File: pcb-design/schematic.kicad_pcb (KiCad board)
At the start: 2 copper layers, 80 parts, among them J1 TempGauge, J2 FuelGauge, J3 SpeedInput_C2_P10-13, J5 SpeedInput_C2_P10-13, J6 SpeedInput_C2_P10-13, Q1 2N2222, Q2 2N2222, Q3 2N2222, Q6 2N2222, Q7 2N2222, Q8 2N3906, Q9 2N3906, U1 ESP32-WROOM-32, U2 MCP23017_SP, U3 MCP2562-E-P

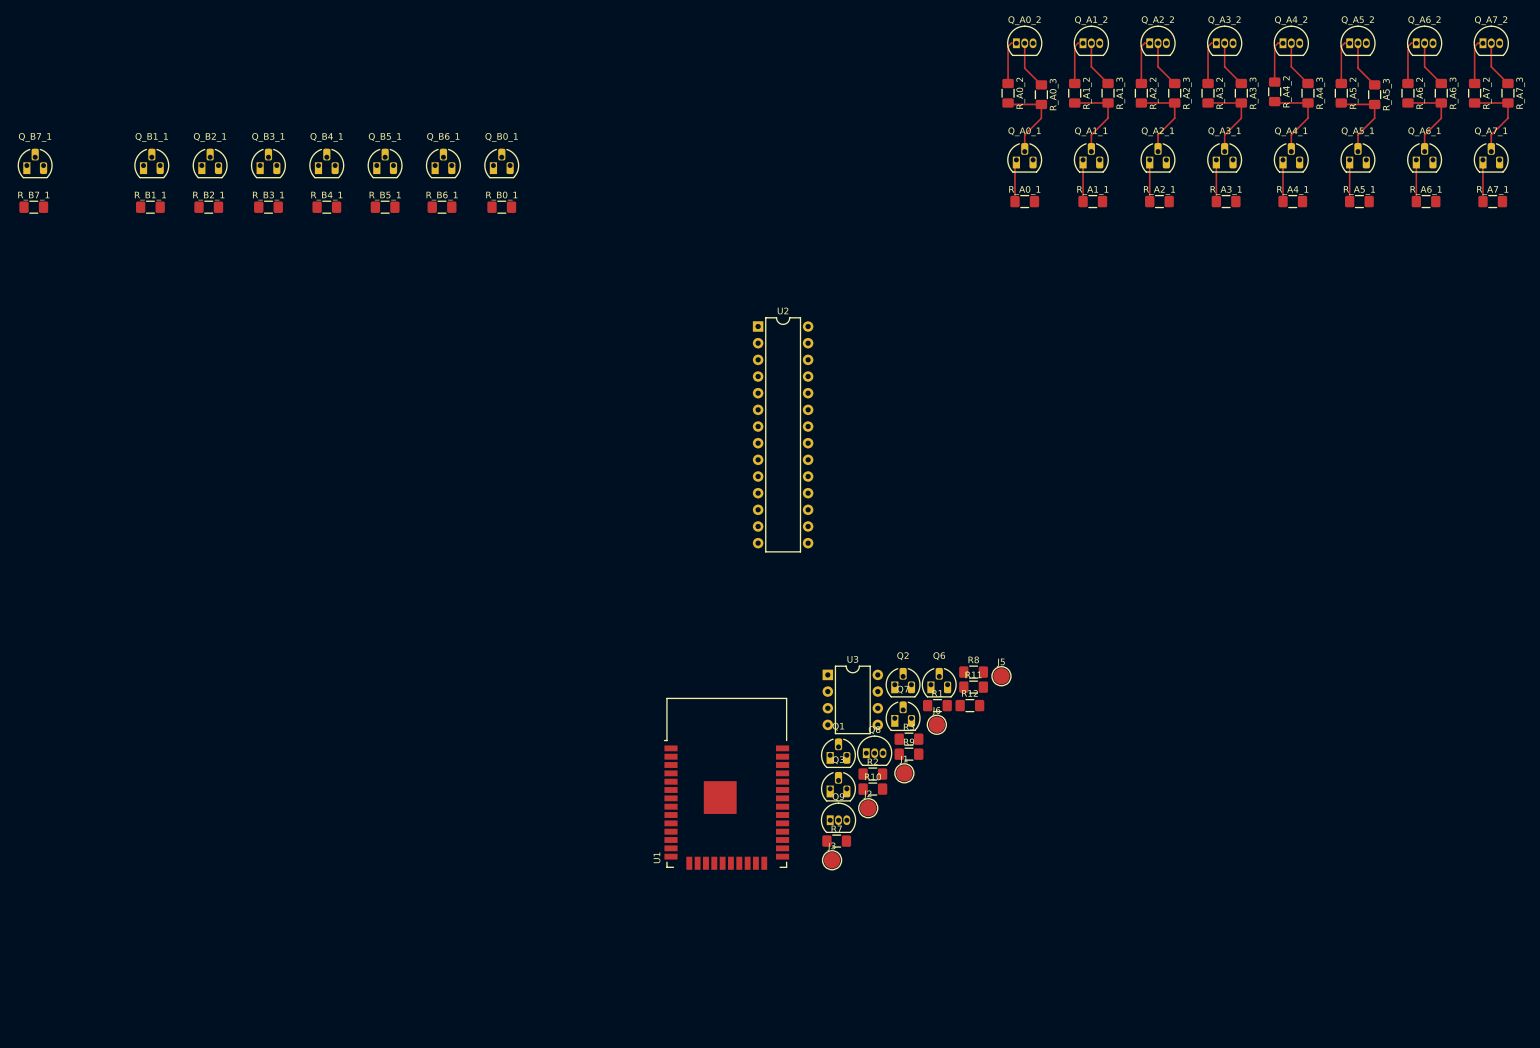
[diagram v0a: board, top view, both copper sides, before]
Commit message: Swapped the esp32 symbol and footprint to be one for the dev modules so I can just populate the boards with standoffs.
Wired up some more nets and made the layout a little prettier.
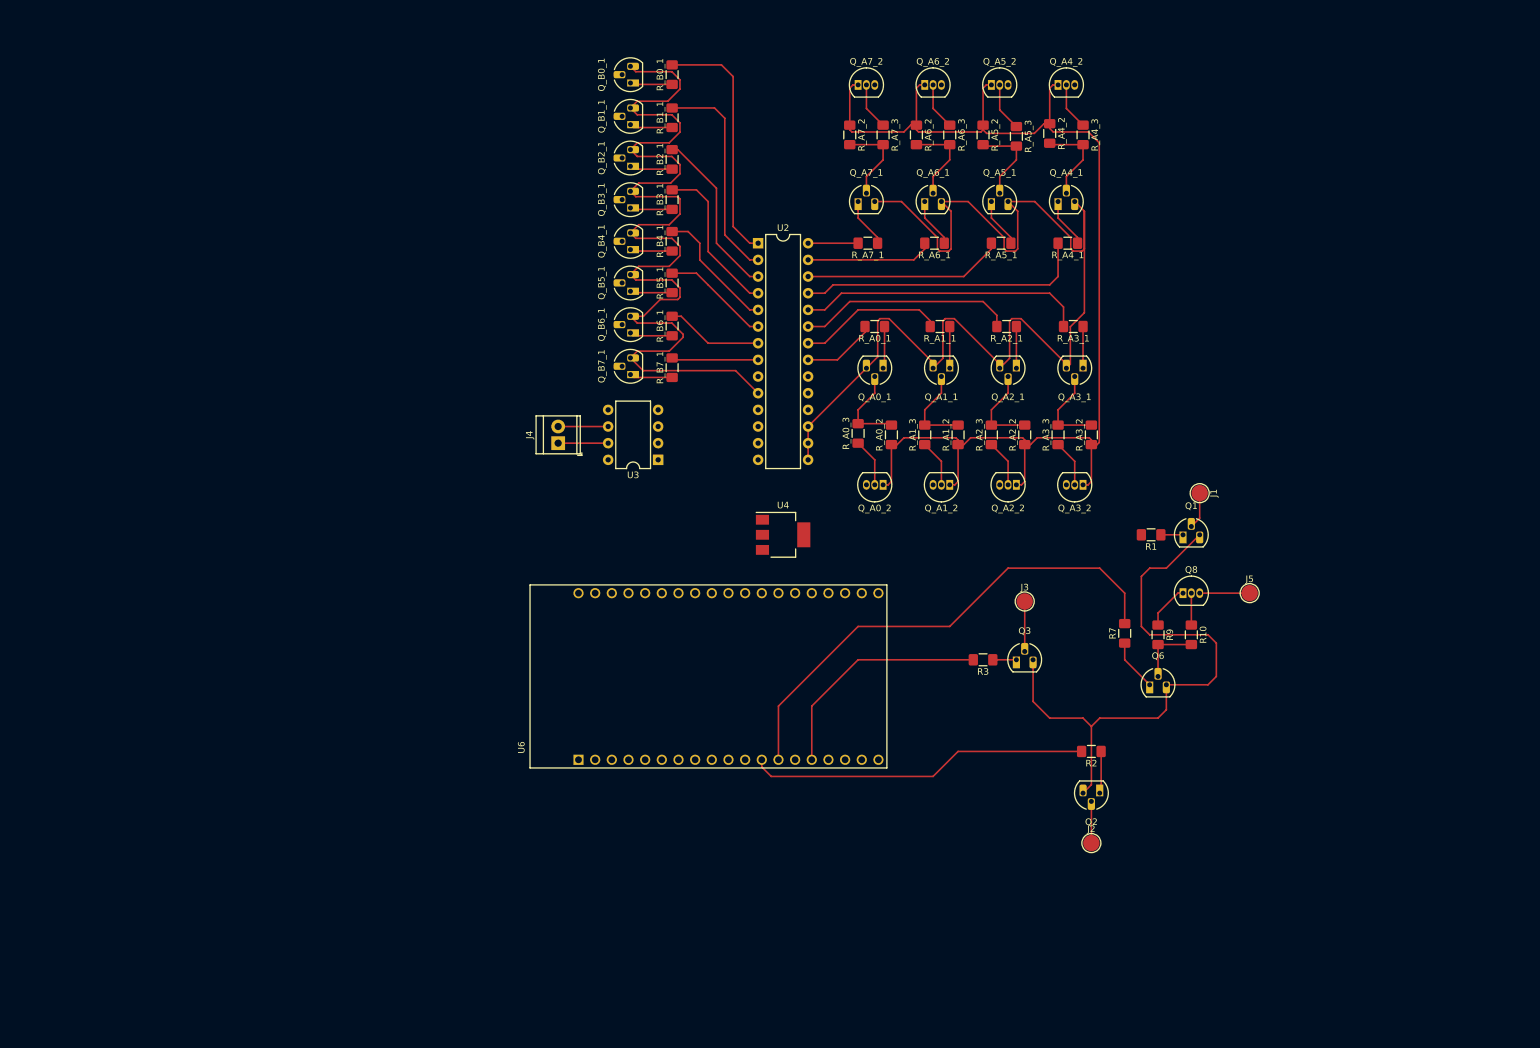
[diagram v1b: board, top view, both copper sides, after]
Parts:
- removed J6: SpeedInput_C2_P10-13, TestPoint:TestPoint_Pad_D2.5mm
- removed Q7: 2N2222, Package_TO_SOT_THT:TO-92_HandSolder
- removed Q9: 2N3906, Package_TO_SOT_THT:TO-92_Inline
- removed R11: 22000, Resistor_SMD:R_1206_3216Metric_Pad1.42x1.75mm_HandSolder
- removed R12, R8: 4000, Resistor_SMD:R_1206_3216Metric_Pad1.42x1.75mm_HandSolder
- removed U1: ESP32-WROOM-32, RF_Module:ESP32-WROOM-32
- added J4: Screw_Terminal_01x02, TerminalBlock_TE-Connectivity:TerminalBlock_TE_282834-2_1x02_P2.54mm_Horizontal, F.Cu at (113.0, 81.3)
- added U4: AP1117-33, Package_TO_SOT_SMD:SOT-223-3_TabPin2, F.Cu at (147.3, 95.2)
- added U6: ESP32-DEVKITC-32D, MODULE_ESP32-DEVKITC-32D, F.Cu at (135.9, 116.8)
- J3: value SpeedInput_C2_P10-13 -> SpeedometerOutput
- J5: value SpeedInput_C2_P10-13 -> TachometerOutput
- moved R_B7_1 100.3 mm to (130.4, 69.8), turned to 90 degrees
- moved Q_B7_1 97.4 mm to (124.1, 70.8), turned to 90 degrees
- moved Q_A7_1 95.5 mm to (158.8, 44.5)
- moved Q_A7_2 95.5 mm to (158.8, 26.7)
- moved R_A7_1 95.5 mm to (160.2, 50.8), turned to 180 degrees
- moved R_A7_2 95.5 mm to (157.5, 34.3)
- moved R_A7_3 95.5 mm to (162.6, 34.3)
- moved R_B1_1 80.7 mm to (130.4, 31.7), turned to 90 degrees
- moved Q_A6_1 75.2 mm to (168.9, 44.5)
- moved Q_A6_2 75.2 mm to (168.9, 26.7)
- moved R_A6_2 75.2 mm to (167.6, 34.3)
- moved R_A6_3 75.2 mm to (172.7, 34.3)
- moved R_A6_1 75.2 mm to (170.4, 50.8), turned to 180 degrees
- moved Q_B1_1 74.5 mm to (124.1, 32.7), turned to 90 degrees
- moved R_B2_1 71.0 mm to (130.4, 38.0), turned to 90 degrees
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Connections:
- R3 pad 2: SpeedometerOutput -> SpeedometerSignal
- U2 pad 12: /Indicator_Lights/SCK -> I2C0_SCK
- U2 pad 13: /Indicator_Lights/SDA -> I2C0_SDA
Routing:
- net GND: track 0.00 -> 415.4 mm
- net +12V: track 56.7 -> 188.4 mm
- net TachometerOutput: track 0.00 -> 75.9 mm
- net FuelOutput: track 0.00 -> 52.0 mm
- net Net-(R_A4_1-Pad2): track 0.00 -> 44.2 mm
- net Net-(R_A3_1-Pad2): track 0.00 -> 43.8 mm
- net Net-(R_B0_1-Pad2): track 0.00 -> 37.8 mm
- net SpeedometerSignal: track 0.00 -> 35.7 mm
- net Net-(R_B1_1-Pad2): track 0.00 -> 33.1 mm
- net Net-(R_A2_1-Pad2): track 0.00 -> 32.9 mm
- net Net-(R_A5_1-Pad2): track 0.00 -> 30.6 mm
- net Net-(R_B2_1-Pad2): track 0.00 -> 26.0 mm
- net Net-(R_B3_1-Pad2): track 0.00 -> 24.1 mm
- net Net-(R_A1_1-Pad2): track 0.00 -> 22.3 mm
- net Net-(R_B4_1-Pad2): track 0.00 -> 19.5 mm
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
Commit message: checkin
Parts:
- moved U4 63.8 mm to (95.2, 132.1)
- moved J2 19.8 mm to (208.3, 156.2)
- moved Q2 19.8 mm to (209.6, 148.6)
- moved R2 19.8 mm to (208.3, 142.2)
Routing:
- net ESP_CAN0_RX: track 0.00 -> 68.1 mm
- net ESP_CAN0_TX: track 0.00 -> 62.0 mm
- net TemperatureOutput: track 0.00 -> 51.4 mm
- net +3V3: track 0.00 -> 41.3 mm
- net I2C0_SCK: track 0.00 -> 34.6 mm
- net I2C0_SDA: track 0.00 -> 28.9 mm
- net FuelOutput: track 52.0 -> 33.2 mm
- net SpeedometerSignal: track 35.7 -> 18.2 mm
- net GND: track 415.4 -> 411.3 mm, vias 0 -> 1

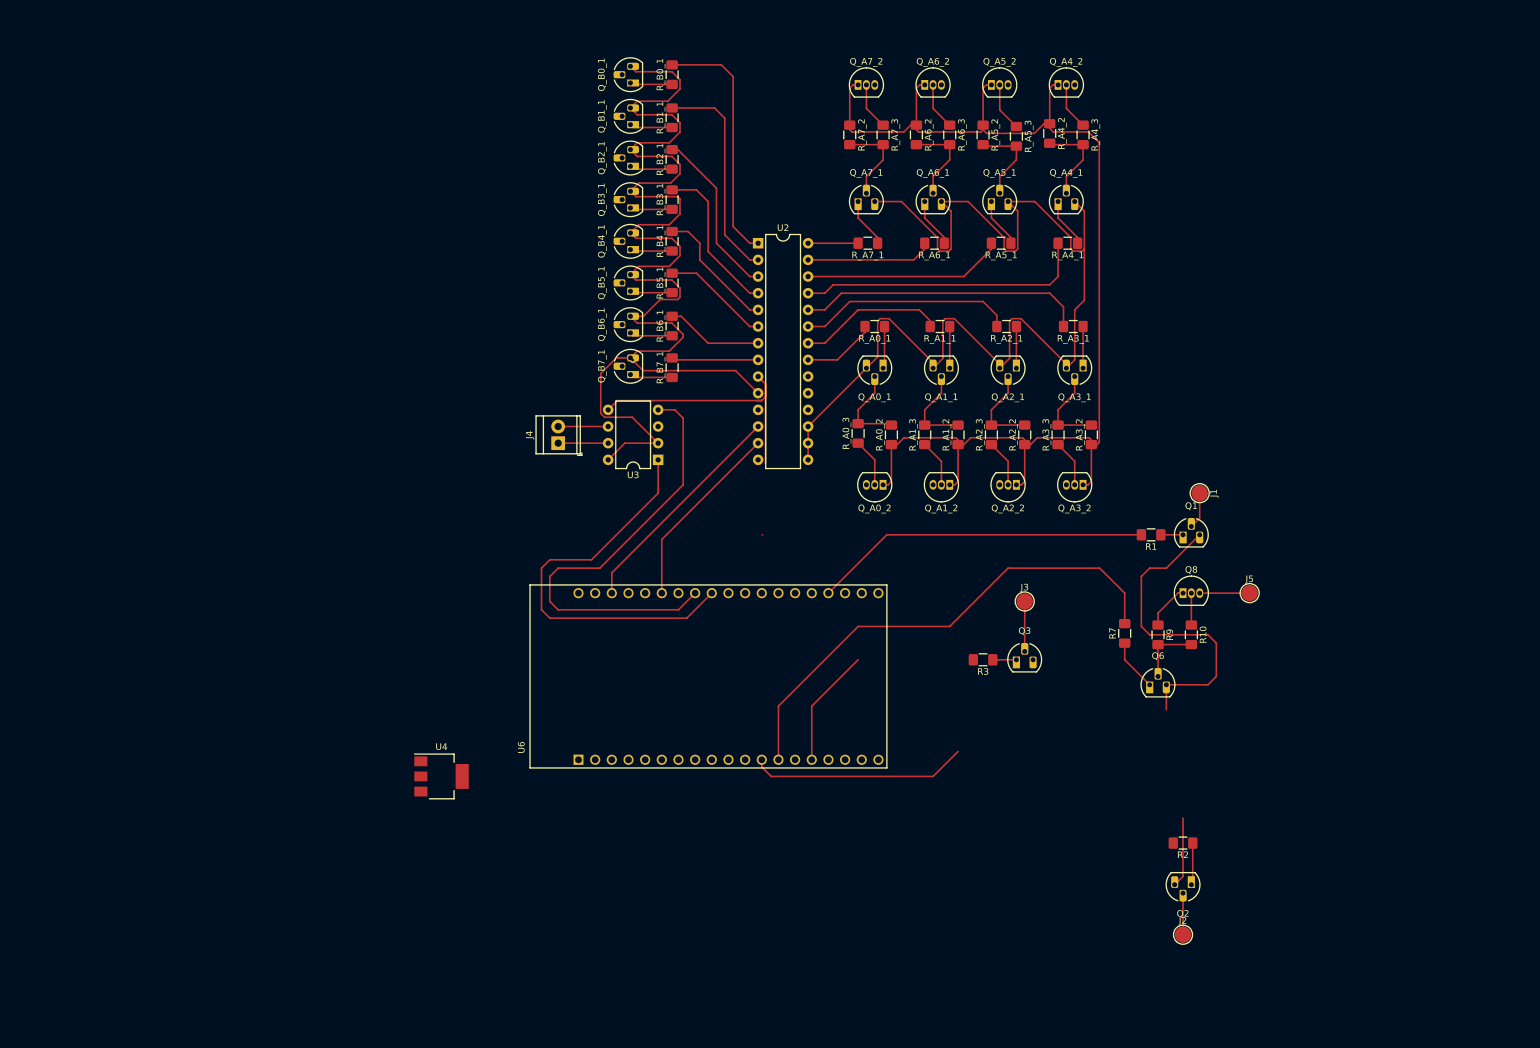
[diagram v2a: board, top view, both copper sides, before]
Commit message: Added TE 827881-1 connector and footprint re-arranged schematic
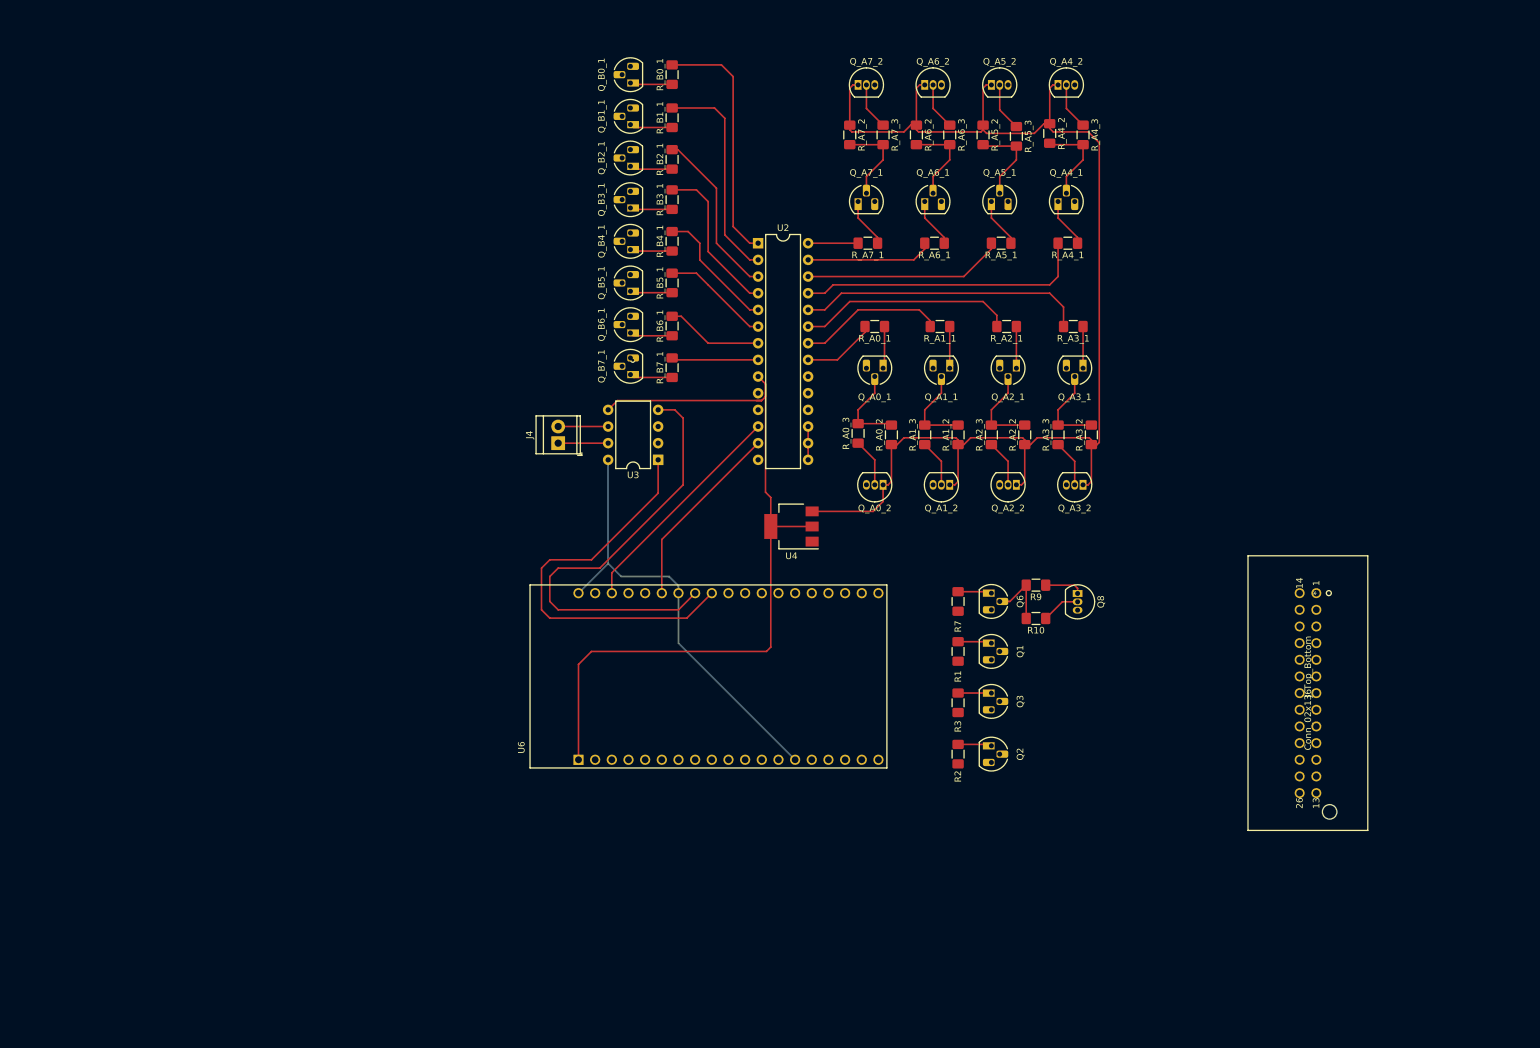
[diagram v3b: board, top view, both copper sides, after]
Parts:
- removed J1: TempGauge, TestPoint:TestPoint_Pad_D2.5mm
- removed J2: FuelGauge, TestPoint:TestPoint_Pad_D2.5mm
- removed J3: SpeedometerOutput, TestPoint:TestPoint_Pad_D2.5mm
- removed J5: TachometerOutput, TestPoint:TestPoint_Pad_D2.5mm
- added J6: Conn_02x13_Top_Bottom, pcb-design:Connector_TE_827881-1, F.Cu at (228.6, 104.1)
- moved U4 65.5 mm to (148.6, 94.0), turned to 180 degrees
- moved Q2 37.1 mm to (179.1, 127.4), turned to 270 degrees
- moved R2 36.9 mm to (174.0, 128.7), turned to 270 degrees
- moved R1 34.4 mm to (174.0, 113.0), turned to 270 degrees
- moved Q1 33.6 mm to (179.1, 111.8), turned to 270 degrees
- moved Q6 27.9 mm to (179.1, 104.1), turned to 270 degrees
- moved R7 25.9 mm to (174.0, 105.4), turned to 270 degrees
- moved R10 23.8 mm to (185.9, 108.0), turned to 180 degrees
- moved R9 20.1 mm to (185.9, 102.9), turned to 180 degrees
- moved Q8 16.1 mm to (192.2, 104.2), turned to 270 degrees
- moved R3 7.58 mm to (174.0, 120.9), turned to 270 degrees
- moved Q3 6.35 mm to (179.1, 119.4), turned to 270 degrees
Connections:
- net Net-(J4-Pad1) renamed CAN0_H
- net Net-(J4-Pad2) renamed CAN0_L
- Q1 pad 2: Net-(J1-Pad1) -> TempGauge
- Q2 pad 2: Net-(J2-Pad1) -> FuelGauge
- Q3 pad 2: Net-(J3-Pad1) -> Speedometer
- Q8 pad 3: Net-(J5-Pad1) -> Tachometer
- Q_A0_2 pad 3: /Indicator_Lights/A0_SourceOutput -> A0_SourceOutput
- Q_A1_2 pad 3: /Indicator_Lights/A1_SourceOutput -> A1_SourceOutput
- Q_A2_2 pad 3: /Indicator_Lights/A2_SourceOutput -> A2_SourceOutput
- Q_A3_2 pad 3: /Indicator_Lights/A3_SourceOutput -> A3_SourceOutput
- Q_A4_2 pad 3: /Indicator_Lights/A4_SourceOutput -> A4_SourceOutput
- Q_A5_2 pad 3: /Indicator_Lights/A5_SourceOutput -> A5_SourceOutput
- Q_A6_2 pad 3: /Indicator_Lights/A6_SourceOutput -> A6_SourceOutput
- Q_A7_2 pad 3: /Indicator_Lights/A7_SourceOutput -> A7_SourceOutput
- Q_B0_1 pad 2: /Indicator_Lights/B0_SinkOutput -> B0_SinkOutput
- Q_B1_1 pad 2: /Indicator_Lights/B1_SinkOutput -> B1_SinkOutput
- Q_B2_1 pad 2: /Indicator_Lights/B2_SinkOutput -> B2_SinkOutput
- Q_B3_1 pad 2: /Indicator_Lights/B3_SinkOutput -> B3_SinkOutput
- Q_B4_1 pad 2: /Indicator_Lights/B4_SinkOutput -> B4_SinkOutput
- Q_B5_1 pad 2: /Indicator_Lights/B5_SinkOutput -> B5_SinkOutput
- Q_B6_1 pad 2: /Indicator_Lights/B6_SinkOutput -> B6_SinkOutput
- Q_B7_1 pad 2: /Indicator_Lights/B7_SinkOutput -> B7_SinkOutput
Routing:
- net GND: track 411.3 -> 75.9 mm
- net +3V3: track 41.3 -> 120.8 mm
- net TachometerOutput: track 75.9 -> 0.00 mm
- net TemperatureOutput: track 51.4 -> 0.00 mm
- net FuelOutput: track 33.2 -> 0.00 mm
- net SpeedometerSignal: track 18.2 -> 0.00 mm
- net +12V: track 188.4 -> 201.3 mm
- net Net-(J5-Pad1): track 7.62 -> 0.00 mm
- net Net-(J3-Pad1): track 7.62 -> 0.00 mm
- net Net-(J2-Pad1): track 6.35 -> 0.00 mm
- net Net-(J1-Pad1): track 5.61 -> 0.00 mm
- net Net-(Q6-Pad1): track 7.93 -> 5.17 mm
- net Net-(Q1-Pad1): track 3.38 -> 5.17 mm
- net Net-(Q3-Pad1): track 3.59 -> 5.09 mm
- net Net-(Q2-Pad1): track 6.44 -> 5.17 mm
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
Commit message: Final changes for Rev 1 board, ordered 10/06/2020
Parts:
- added U7: L7805, Package_SIP:SIP3_11.6x8.5mm, F.Cu at (96.5, 147.3)
- U4: footprint Package_TO_SOT_SMD:SOT-223-3_TabPin2 -> Package_SIP:SIP3_11.6x8.5mm
- moved J4 80.8 mm to (136.6, 158.6), turned to 180 degrees
- moved J6 72.3 mm to (160.0, 127.0)
- moved Q1 70.8 mm to (119.4, 149.9)
- moved R1 70.8 mm to (114.3, 151.1)
- moved U6 67.3 mm to (69.8, 129.5), turned to 180 degrees
- moved R10 63.9 mm to (126.2, 130.9)
- moved R7 63.9 mm to (114.3, 128.3)
- moved R3 63.9 mm to (114.3, 143.7)
- moved R9 63.9 mm to (126.2, 125.8)
- moved Q3 63.9 mm to (119.4, 142.2)
- moved Q6 63.9 mm to (119.4, 127.0)
- moved Q8 63.9 mm to (132.5, 127.1)
- moved R_B4_1 61.9 mm to (74.5, 77.2)
- moved R_A0_2 61.9 mm to (108.0, 106.7)
- moved R_A1_2 61.9 mm to (118.1, 106.7)
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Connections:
- J6 pad 1: A0_SourceOutput -> B0_SinkOutput
- J6 pad 14: B0_SinkOutput -> A7_SourceOutput
- J6 pad 15: B1_SinkOutput -> A6_SourceOutput
- J6 pad 16: B2_SinkOutput -> A5_SourceOutput
- J6 pad 17: B3_SinkOutput -> A4_SourceOutput
- J6 pad 18: B4_SinkOutput -> A3_SourceOutput
- J6 pad 19: B5_SinkOutput -> A2_SourceOutput
- J6 pad 2: A1_SourceOutput -> B1_SinkOutput
- J6 pad 20: B6_SinkOutput -> A1_SourceOutput
- J6 pad 21: B7_SinkOutput -> A0_SourceOutput
- J6 pad 22: TempGauge -> Tachometer
- J6 pad 23: Tachometer -> FuelGauge
- J6 pad 25: FuelGauge -> TempGauge
- J6 pad 3: A2_SourceOutput -> B2_SinkOutput
- J6 pad 4: A3_SourceOutput -> B3_SinkOutput
- J6 pad 5: A4_SourceOutput -> B4_SinkOutput
- J6 pad 6: A5_SourceOutput -> B5_SinkOutput
- J6 pad 7: A6_SourceOutput -> B6_SinkOutput
- J6 pad 8: A7_SourceOutput -> B7_SinkOutput
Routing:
- net B7_SinkOutput: track 0.00 -> 278.3 mm
- net B6_SinkOutput: track 0.00 -> 264.0 mm
- net B5_SinkOutput: track 0.00 -> 249.8 mm
- net B4_SinkOutput: track 0.00 -> 235.5 mm
- net B3_SinkOutput: track 0.00 -> 221.2 mm
- net B2_SinkOutput: track 0.00 -> 206.9 mm
- net B1_SinkOutput: track 0.00 -> 192.7 mm
- net B0_SinkOutput: track 0.00 -> 173.1 mm
- net A7_SourceOutput: track 0.00 -> 135.8 mm
- net A6_SourceOutput: track 0.00 -> 124.1 mm
- net +12V: track 201.3 -> 324.9 mm
- net A5_SourceOutput: track 0.00 -> 111.7 mm
- net TemperatureOutput: track 0.00 -> 101.8 mm
- net A4_SourceOutput: track 0.00 -> 93.9 mm
- net SpeedometerSignal: track 0.00 -> 90.4 mm
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- added copper zone on B.Cu, net +12V
- added copper zone on B.Cu, net GND
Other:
- board outline added: 130.8 x 139.7 mm
- board text added: "E28 CLUSTER DRIVER REV 1. BRADY DOW"
